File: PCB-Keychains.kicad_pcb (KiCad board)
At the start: 2 copper layers, 79.1 x 91.4 mm, 245 parts

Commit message: Add a bunch of layouts
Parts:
- added REF**: Pad-1U, locallib:Pad-1U, F.Cu at (115.3, 79.1)
- added REF**: Pad-1U, locallib:Pad-1U, F.Cu at (145.7, 79.1)
- added REF**: Pad-1U, locallib:Pad-1U, F.Cu at (174.3, 100.0)
- added REF**: Pad-1U, locallib:Pad-1U, F.Cu at (123.8, 100.0)
- added REF**: Pad-1U, locallib:Pad-1U, F.Cu at (135.3, 100.0)
- added REF**: Pad-2.75U, locallib:Pad-2.75U, F.Cu at (161.4, 100.0)
- added REF**: Pad-1U, locallib:Pad-1U, F.Cu at (146.7, 100.0)
- added REF**: Pad-1U, locallib:Pad-1U, F.Cu at (127.6, 100.0)
- added REF**: Pad-1U, locallib:Pad-1U, F.Cu at (150.5, 100.0)
- added REF**: Pad-1U, locallib:Pad-1U, F.Cu at (178.1, 100.0)
- added REF**: Pad-1U, locallib:Pad-1U, F.Cu at (120.0, 100.0)
- added REF**: Pad-1U, locallib:Pad-1U, F.Cu at (170.5, 88.6)
- added REF**: Pad-1U, locallib:Pad-1U, F.Cu at (119.1, 79.1)
- added REF**: Pad-1.5U, locallib:Pad-1.5U, F.Cu at (121.9, 103.8)
- added REF**: Pad-1U, locallib:Pad-1U, F.Cu at (178.1, 88.6)
- added REF**: Pad-1U, locallib:Pad-1U, F.Cu at (174.3, 88.6)
- added REF**: Pad-1U, locallib:Pad-1U, F.Cu at (131.4, 100.0)
- added REF**: Pad-1U, locallib:Pad-1U, F.Cu at (174.3, 96.2)
- added REF**: Pad-2.25U, locallib:Pad-2.25U, F.Cu at (113.8, 100.0)
- added REF**: Pad-1U, locallib:Pad-1U, F.Cu at (133.3, 96.2)
- added REF**: Pad-1.5U, locallib:Pad-1.5U, F.Cu at (163.8, 103.8)
- added REF**: Pad-1U, locallib:Pad-1U, F.Cu at (170.5, 92.4)
- added REF**: Pad-1U, locallib:Pad-1U, F.Cu at (115.3, 88.6)
- added REF**: Pad-1U, locallib:Pad-1U, F.Cu at (134.3, 79.1)
- added REF**: Pad-1U, locallib:Pad-1U, F.Cu at (226.7, 26.7)
- added REF**: Pad-1U, locallib:Pad-1U, F.Cu at (226.7, 30.5)
- added REF**: Pad-1U, locallib:Pad-1U, F.Cu at (226.7, 19.1)
- added REF**: Pad-1U, locallib:Pad-1U, F.Cu at (230.5, 26.7)
- added REF**: Pad-1U, locallib:Pad-1U, F.Cu at (230.5, 34.3)
- added REF**: Pad-1U, locallib:Pad-1U, F.Cu at (226.7, 22.9)
- added REF**: Pad-1U, locallib:Pad-1U, F.Cu at (230.5, 19.1)
- added REF**: Pad-1U, locallib:Pad-1U, F.Cu at (230.5, 30.5)
- added REF**: Pad-1U, locallib:Pad-1U, F.Cu at (226.7, 34.3)
- added REF**: Pad-1U, locallib:Pad-1U, F.Cu at (230.5, 22.9)
- added REF**: Pad-1U, locallib:Pad-1U, F.Cu at (115.3, 82.9)
- added REF**: Pad-1U, locallib:Pad-1U, F.Cu at (266.7, 30.5)
- added REF**: Pad-1U, locallib:Pad-1U, F.Cu at (255.3, 30.5)
- added REF**: Pad-1U, locallib:Pad-1U, F.Cu at (262.9, 30.5)
- added REF**: Pad-1.5U, locallib:Pad-1.5U, F.Cu at (287.7, 34.3)
- added REF**: Pad-1U, locallib:Pad-1U, F.Cu at (270.5, 30.5)
- added REF**: Pad-1.5U, locallib:Pad-1.5U, F.Cu at (278.1, 34.3)
- added REF**: Pad-1U, locallib:Pad-1U, F.Cu at (259.1, 30.5)
- added REF**: Pad-1.5U, locallib:Pad-1.5U, F.Cu at (236.2, 22.9)
- added REF**: Pad-2.75U, locallib:Pad-2.75U, F.Cu at (285.3, 30.5)
- added REF**: Pad-7U, locallib:Pad-7U, F.Cu at (261.9, 34.3)
- added REF**: Pad-1U, locallib:Pad-1U, F.Cu at (149.5, 82.9)
- added REF**: Pad-1.75U, locallib:Pad-1.75U, F.Cu at (236.7, 26.7)
- added REF**: Pad-1.5U, locallib:Pad-1.5U, F.Cu at (287.7, 22.9)
- added REF**: Pad-2U, locallib:Pad-2U, F.Cu at (286.7, 19.1)
- added REF**: Pad-2.25U, locallib:Pad-2.25U, F.Cu at (286.2, 26.7)
- added REF**: Pad-1.5U, locallib:Pad-1.5U, F.Cu at (236.2, 34.3)
- added REF**: Pad-2.25U, locallib:Pad-2.25U, F.Cu at (237.6, 30.5)
- added REF**: Pad-1.5U, locallib:Pad-1.5U, F.Cu at (245.7, 34.3)
- added REF**: Pad-1U, locallib:Pad-1U, F.Cu at (235.3, 19.1)
- added REF**: Pad-1U, locallib:Pad-1U, F.Cu at (246.7, 19.1)
- added REF**: Pad-1U, locallib:Pad-1U, F.Cu at (242.9, 19.1)
- added REF**: Pad-1U, locallib:Pad-1U, F.Cu at (130.5, 82.9)
- added REF**: Pad-1U, locallib:Pad-1U, F.Cu at (250.5, 19.1)
- added REF**: Pad-1U, locallib:Pad-1U, F.Cu at (277.2, 19.1)
- added REF**: Pad-1U, locallib:Pad-1U, F.Cu at (278.1, 30.5)
- added REF**: Pad-1U, locallib:Pad-1U, F.Cu at (271.5, 22.9)
- added REF**: Pad-1U, locallib:Pad-1U, F.Cu at (263.8, 22.9)
- added REF**: Pad-1U, locallib:Pad-1U, F.Cu at (253.4, 26.7)
- added REF**: Pad-1U, locallib:Pad-1U, F.Cu at (264.8, 26.7)
- added REF**: Pad-1U, locallib:Pad-1U, F.Cu at (261.0, 26.7)
- added REF**: Pad-1U, locallib:Pad-1U, F.Cu at (241.9, 26.7)
- added REF**: Pad-1U, locallib:Pad-1U, F.Cu at (280.0, 26.7)
- added REF**: Pad-1U, locallib:Pad-1U, F.Cu at (122.9, 82.9)
- added REF**: Pad-1U, locallib:Pad-1U, F.Cu at (249.6, 26.7)
- added REF**: Pad-1U, locallib:Pad-1U, F.Cu at (247.7, 30.5)
- added REF**: Pad-1U, locallib:Pad-1U, F.Cu at (274.3, 30.5)
- added REF**: Pad-1U, locallib:Pad-1U, F.Cu at (248.6, 22.9)
- added REF**: Pad-1U, locallib:Pad-1U, F.Cu at (275.3, 22.9)
- added REF**: Pad-1U, locallib:Pad-1U, F.Cu at (256.2, 22.9)
- added REF**: Pad-1U, locallib:Pad-1U, F.Cu at (272.4, 26.7)
- added REF**: Pad-1U, locallib:Pad-1U, F.Cu at (258.1, 19.1)
- added REF**: Pad-1U, locallib:Pad-1U, F.Cu at (261.9, 19.1)
- added REF**: Pad-1U, locallib:Pad-1U, F.Cu at (282.9, 22.9)
- added REF**: Pad-1U, locallib:Pad-1U, F.Cu at (126.7, 82.9)
- added REF**: Pad-1U, locallib:Pad-1U, F.Cu at (257.2, 26.7)
- added REF**: Pad-1U, locallib:Pad-1U, F.Cu at (267.7, 22.9)
- added REF**: Pad-1U, locallib:Pad-1U, F.Cu at (269.6, 19.1)
- added REF**: Pad-1U, locallib:Pad-1U, F.Cu at (243.8, 30.5)
- added REF**: Pad-1U, locallib:Pad-1U, F.Cu at (244.8, 22.9)
- added REF**: Pad-1U, locallib:Pad-1U, F.Cu at (260.0, 22.9)
- added REF**: Pad-1U, locallib:Pad-1U, F.Cu at (252.4, 22.9)
- added REF**: Pad-1U, locallib:Pad-1U, F.Cu at (245.7, 26.7)
- added REF**: Pad-1U, locallib:Pad-1U, F.Cu at (265.7, 19.1)
- added REF**: Pad-1U, locallib:Pad-1U, F.Cu at (268.6, 26.7)
- added REF**: Pad-1U, locallib:Pad-1U, F.Cu at (138.1, 82.9)
- added REF**: Pad-1U, locallib:Pad-1U, F.Cu at (279.1, 22.9)
- added REF**: Pad-1U, locallib:Pad-1U, F.Cu at (251.5, 30.5)
- added REF**: Pad-1U, locallib:Pad-1U, F.Cu at (239.1, 19.1)
- added REF**: Pad-1U, locallib:Pad-1U, F.Cu at (276.2, 26.7)
- added REF**: Pad-1U, locallib:Pad-1U, F.Cu at (254.3, 19.1)
- added REF**: Pad-1U, locallib:Pad-1U, F.Cu at (273.4, 19.1)
- added REF**: Pad-1U, locallib:Pad-1U, F.Cu at (281.0, 19.1)
- added REF**: Pad-1U, locallib:Pad-1U, F.Cu at (241.0, 22.9)
- added REF**: Pad-1.25U, locallib:Pad-1.25U, F.Cu at (97.6, 66.7)
- added REF**: Pad-1.25U, locallib:Pad-1.25U, F.Cu at (135.7, 66.7)
- added REF**: Pad-1U, locallib:Pad-1U, F.Cu at (141.9, 82.9)
- added REF**: Pad-1.25U, locallib:Pad-1.25U, F.Cu at (140.5, 66.7)
- added REF**: Pad-6.25U, locallib:Pad-6.25U, F.Cu at (121.4, 66.7)
- added REF**: Pad-1.25U, locallib:Pad-1.25U, F.Cu at (102.4, 66.7)
- added REF**: Pad-1.25U, locallib:Pad-1.25U, F.Cu at (107.2, 66.7)
- added REF**: Pad-1U, locallib:Pad-1U, F.Cu at (174.3, 58.1)
- added REF**: Pad-1U, locallib:Pad-1U, F.Cu at (204.8, 58.1)
- added REF**: Pad-1U, locallib:Pad-1U, F.Cu at (193.4, 58.1)
- added REF**: Pad-1U, locallib:Pad-1U, F.Cu at (208.6, 58.1)
- added REF**: Pad-1U, locallib:Pad-1U, F.Cu at (197.2, 58.1)
- added REF**: Pad-1U, locallib:Pad-1U, F.Cu at (178.1, 58.1)
- added REF**: Pad-1U, locallib:Pad-1U, F.Cu at (149.5, 79.1)
- added REF**: Pad-1U, locallib:Pad-1U, F.Cu at (157.2, 82.9)
- added REF**: Pad-1U, locallib:Pad-1U, F.Cu at (170.5, 58.1)
- added REF**: Pad-1U, locallib:Pad-1U, F.Cu at (201.0, 58.1)
- added REF**: Pad-1U, locallib:Pad-1U, F.Cu at (181.9, 58.1)
- added REF**: Pad-1U, locallib:Pad-1U, F.Cu at (166.7, 58.1)
- added REF**: Pad-1U, locallib:Pad-1U, F.Cu at (174.3, 54.3)
- added REF**: Pad-1U, locallib:Pad-1U, F.Cu at (204.8, 54.3)
- added REF**: Pad-1U, locallib:Pad-1U, F.Cu at (189.5, 54.3)
- added REF**: Pad-1U, locallib:Pad-1U, F.Cu at (193.4, 54.3)
- added REF**: Pad-1U, locallib:Pad-1U, F.Cu at (208.6, 54.3)
- added REF**: Pad-1U, locallib:Pad-1U, F.Cu at (197.2, 54.3)
- added REF**: Pad-1U, locallib:Pad-1U, F.Cu at (153.4, 82.9)
- added REF**: Pad-1U, locallib:Pad-1U, F.Cu at (178.1, 54.3)
- added REF**: Pad-1U, locallib:Pad-1U, F.Cu at (170.5, 54.3)
- added REF**: Pad-1U, locallib:Pad-1U, F.Cu at (201.0, 54.3)
- added REF**: Pad-1U, locallib:Pad-1U, F.Cu at (181.9, 54.3)
- added REF**: Pad-1U, locallib:Pad-1U, F.Cu at (185.7, 54.3)
- added REF**: Pad-1U, locallib:Pad-1U, F.Cu at (166.7, 54.3)
- added REF**: Pad-1U, locallib:Pad-1U, F.Cu at (174.3, 50.5)
- added REF**: Pad-1U, locallib:Pad-1U, F.Cu at (204.8, 50.5)
- added REF**: Pad-1U, locallib:Pad-1U, F.Cu at (189.5, 50.5)
- added REF**: Pad-1U, locallib:Pad-1U, F.Cu at (193.4, 50.5)
- added REF**: Pad-1U, locallib:Pad-1U, F.Cu at (145.7, 82.9)
- added REF**: Pad-1U, locallib:Pad-1U, F.Cu at (208.6, 50.5)
- added REF**: Pad-1U, locallib:Pad-1U, F.Cu at (197.2, 50.5)
- added REF**: Pad-1U, locallib:Pad-1U, F.Cu at (178.1, 50.5)
- added REF**: Pad-1U, locallib:Pad-1U, F.Cu at (170.5, 50.5)
- added REF**: Pad-1U, locallib:Pad-1U, F.Cu at (201.0, 50.5)
- added REF**: Pad-1U, locallib:Pad-1U, F.Cu at (181.9, 50.5)
- added REF**: Pad-1U, locallib:Pad-1U, F.Cu at (185.7, 50.5)
- added REF**: Pad-1U, locallib:Pad-1U, F.Cu at (166.7, 50.5)
- added REF**: Pad-1U, locallib:Pad-1U, F.Cu at (174.3, 46.7)
- added REF**: Pad-1U, locallib:Pad-1U, F.Cu at (204.8, 46.7)
- added REF**: Pad-1U, locallib:Pad-1U, F.Cu at (119.1, 82.9)
- added REF**: Pad-1U, locallib:Pad-1U, F.Cu at (189.5, 46.7)
- added REF**: Pad-1U, locallib:Pad-1U, F.Cu at (193.4, 46.7)
- added REF**: Pad-1U, locallib:Pad-1U, F.Cu at (208.6, 46.7)
- added REF**: Pad-1U, locallib:Pad-1U, F.Cu at (197.2, 46.7)
- added REF**: Pad-1U, locallib:Pad-1U, F.Cu at (178.1, 46.7)
- added REF**: Pad-1U, locallib:Pad-1U, F.Cu at (170.5, 46.7)
- added REF**: Pad-1U, locallib:Pad-1U, F.Cu at (201.0, 46.7)
- added REF**: Pad-1U, locallib:Pad-1U, F.Cu at (181.9, 46.7)
- added REF**: Pad-1U, locallib:Pad-1U, F.Cu at (185.7, 46.7)
- added REF**: Pad-1U, locallib:Pad-1U, F.Cu at (166.7, 46.7)
- added REF**: Pad-1U, locallib:Pad-1U, F.Cu at (134.3, 82.9)
- added REF**: Pad-1U, locallib:Pad-1U, F.Cu at (106.7, 46.7)
- added REF**: Pad-1U, locallib:Pad-1U, F.Cu at (122.9, 46.7)
- added REF**: Pad-1U, locallib:Pad-1U, F.Cu at (130.5, 46.7)
- added REF**: Pad-1U, locallib:Pad-1U, F.Cu at (142.9, 46.7)
- added REF**: Pad-1U, locallib:Pad-1U, F.Cu at (135.3, 46.7)
- added REF**: Pad-1U, locallib:Pad-1U, F.Cu at (119.1, 46.7)
- added REF**: Pad-1U, locallib:Pad-1U, F.Cu at (146.7, 46.7)
- added REF**: Pad-1U, locallib:Pad-1U, F.Cu at (114.3, 46.7)
- added REF**: Pad-1U, locallib:Pad-1U, F.Cu at (126.7, 46.7)
- added REF**: Pad-1U, locallib:Pad-1U, F.Cu at (139.1, 46.7)
- added REF**: Pad-1U, locallib:Pad-1U, F.Cu at (191.5, 103.8)
- added REF**: Pad-1U, locallib:Pad-1U, F.Cu at (110.5, 46.7)
- added REF**: Pad-1U, locallib:Pad-1U, F.Cu at (102.9, 46.7)
- added REF**: Pad-1U, locallib:Pad-1U, F.Cu at (97.2, 46.7)
- added REF**: Pad-1U, locallib:Pad-1U, F.Cu at (154.3, 59.1)
- added REF**: Pad-1U, locallib:Pad-1U, F.Cu at (154.3, 62.9)
- added REF**: Pad-1.75U, locallib:Pad-1.75U, F.Cu at (145.3, 62.9)
- added REF**: Pad-1U, locallib:Pad-1U, F.Cu at (104.8, 51.4)
- added REF**: Pad-1U, locallib:Pad-1U, F.Cu at (135.3, 51.4)
- added REF**: Pad-1U, locallib:Pad-1U, F.Cu at (114.3, 55.2)
- added REF**: Pad-1U, locallib:Pad-1U, F.Cu at (120.0, 51.4)
- added REF**: Pad-1U, locallib:Pad-1U, F.Cu at (191.5, 96.2)
- added REF**: Pad-1U, locallib:Pad-1U, F.Cu at (154.3, 51.4)
- added REF**: Pad-1U, locallib:Pad-1U, F.Cu at (154.3, 55.2)
- added REF**: Pad-1U, locallib:Pad-1U, F.Cu at (102.9, 55.2)
- added REF**: Pad-2.25U, locallib:Pad-2.25U, F.Cu at (148.1, 59.1)
- added REF**: Pad-1U, locallib:Pad-1U, F.Cu at (125.7, 55.2)
- added REF**: Pad-1U, locallib:Pad-1U, F.Cu at (122.9, 59.1)
- added REF**: Pad-1U, locallib:Pad-1U, F.Cu at (150.5, 62.9)
- added REF**: Pad-1U, locallib:Pad-1U, F.Cu at (150.5, 66.7)
- added REF**: Pad-1U, locallib:Pad-1U, F.Cu at (117.2, 62.9)
- added REF**: Pad-1.5U, locallib:Pad-1.5U, F.Cu at (98.1, 55.2)
- added REF**: Pad-1U, locallib:Pad-1U, F.Cu at (191.5, 88.6)
- added REF**: Pad-1U, locallib:Pad-1U, F.Cu at (123.8, 51.4)
- added REF**: Pad-1U, locallib:Pad-1U, F.Cu at (154.3, 66.7)
- added REF**: Pad-1U, locallib:Pad-1U, F.Cu at (139.1, 51.4)
- added REF**: Pad-1U, locallib:Pad-1U, F.Cu at (127.6, 51.4)
- added REF**: Pad-1U, locallib:Pad-1U, F.Cu at (108.6, 51.4)
- added REF**: Pad-1U, locallib:Pad-1U, F.Cu at (121.9, 55.2)
- added REF**: Pad-1U, locallib:Pad-1U, F.Cu at (144.8, 55.2)
- added REF**: Pad-1U, locallib:Pad-1U, F.Cu at (106.7, 55.2)
- added REF**: Pad-1U, locallib:Pad-1U, F.Cu at (133.3, 55.2)
- added REF**: Pad-2U, locallib:Pad-2U, F.Cu at (148.6, 51.4)
- added REF**: Pad-1U, locallib:Pad-1U, F.Cu at (191.5, 92.4)
- added REF**: Pad-1U, locallib:Pad-1U, F.Cu at (115.3, 59.1)
- added REF**: Pad-1U, locallib:Pad-1U, F.Cu at (101.0, 51.4)
- added REF**: Pad-1U, locallib:Pad-1U, F.Cu at (121.0, 62.9)
- added REF**: Pad-1U, locallib:Pad-1U, F.Cu at (137.2, 55.2)
- added REF**: Pad-1U, locallib:Pad-1U, F.Cu at (107.6, 59.1)
- added REF**: Pad-1U, locallib:Pad-1U, F.Cu at (131.4, 51.4)
- added REF**: Pad-1U, locallib:Pad-1U, F.Cu at (112.4, 51.4)
- added REF**: Pad-1U, locallib:Pad-1U, F.Cu at (132.4, 62.9)
- added REF**: Pad-1U, locallib:Pad-1U, F.Cu at (116.2, 51.4)
- added REF**: Pad-1U, locallib:Pad-1U, F.Cu at (126.7, 59.1)
- added REF**: Pad-1U, locallib:Pad-1U, F.Cu at (191.5, 100.0)
- added REF**: Pad-1U, locallib:Pad-1U, F.Cu at (146.7, 66.7)
- added REF**: Pad-2.25U, locallib:Pad-2.25U, F.Cu at (99.5, 62.9)
- added REF**: Pad-1U, locallib:Pad-1U, F.Cu at (124.8, 62.9)
- added REF**: Pad-1.5U, locallib:Pad-1.5U, F.Cu at (149.5, 55.2)
- added REF**: Pad-1U, locallib:Pad-1U, F.Cu at (109.5, 62.9)
- added REF**: Pad-1U, locallib:Pad-1U, F.Cu at (134.3, 59.1)
- added REF**: Pad-1U, locallib:Pad-1U, F.Cu at (118.1, 55.2)
- added REF**: Pad-1U, locallib:Pad-1U, F.Cu at (97.2, 51.4)
- added REF**: Pad-1U, locallib:Pad-1U, F.Cu at (141.9, 59.1)
- added REF**: Pad-1U, locallib:Pad-1U, F.Cu at (105.7, 62.9)
- added REF**: Pad-1U, locallib:Pad-1U, F.Cu at (130.5, 79.1)
- added REF**: Pad-1U, locallib:Pad-1U, F.Cu at (195.3, 88.6)
- added REF**: Pad-1U, locallib:Pad-1U, F.Cu at (119.1, 59.1)
- added REF**: Pad-1U, locallib:Pad-1U, F.Cu at (111.4, 59.1)
- added REF**: Pad-1U, locallib:Pad-1U, F.Cu at (140.0, 62.9)
- added REF**: Pad-1U, locallib:Pad-1U, F.Cu at (136.2, 62.9)
- added REF**: Pad-1U, locallib:Pad-1U, F.Cu at (113.3, 62.9)
- added REF**: Pad-1U, locallib:Pad-1U, F.Cu at (128.6, 62.9)
- added REF**: Pad-1U, locallib:Pad-1U, F.Cu at (138.1, 59.1)
- added REF**: Pad-1.75U, locallib:Pad-1.75U, F.Cu at (98.6, 59.1)
- added REF**: Pad-1U, locallib:Pad-1U, F.Cu at (130.5, 59.1)
- added REF**: Pad-1U, locallib:Pad-1U, F.Cu at (129.5, 55.2)
- added REF**: Pad-1U, locallib:Pad-1U, F.Cu at (187.6, 103.8)
- added REF**: Pad-1U, locallib:Pad-1U, F.Cu at (141.0, 55.2)
- added REF**: Pad-1U, locallib:Pad-1U, F.Cu at (110.5, 55.2)
- added REF**: Pad-1U, locallib:Pad-1U, F.Cu at (103.8, 59.1)
- added REF**: Pad-1U, locallib:Pad-1U, F.Cu at (142.9, 51.4)
- added REF**: Pad-1U, locallib:Pad-1U, F.Cu at (214.3, 26.7)
- added REF**: Pad-1U, locallib:Pad-1U, F.Cu at (214.3, 30.5)
- added REF**: Pad-1U, locallib:Pad-1U, F.Cu at (168.6, 19.1)
- added REF**: Pad-1U, locallib:Pad-1U, F.Cu at (181.9, 22.9)
- added REF**: Pad-1U, locallib:Pad-1U, F.Cu at (204.8, 22.9)
- added REF**: Pad-1U, locallib:Pad-1U, F.Cu at (191.5, 19.1)
- added REF**: Pad-1U, locallib:Pad-1U, F.Cu at (183.8, 103.8)
- added REF**: Pad-1.5U, locallib:Pad-1.5U, F.Cu at (158.1, 22.9)
- added REF**: Pad-1U, locallib:Pad-1U, F.Cu at (164.8, 19.1)
- added REF**: Pad-1U, locallib:Pad-1U, F.Cu at (195.3, 19.1)
- added REF**: Pad-1U, locallib:Pad-1U, F.Cu at (174.3, 22.9)
- added REF**: Pad-1U, locallib:Pad-1U, F.Cu at (180.0, 19.1)
- added REF**: Pad-1U, locallib:Pad-1U, F.Cu at (172.4, 19.1)
- added REF**: Pad-1U, locallib:Pad-1U, F.Cu at (161.0, 19.1)
- added REF**: Pad-1U, locallib:Pad-1U, F.Cu at (183.8, 19.1)
- added REF**: Pad-1U, locallib:Pad-1U, F.Cu at (176.2, 19.1)
- added REF**: Pad-1U, locallib:Pad-1U, F.Cu at (166.7, 22.9)
- added REF**: Pad-1U, locallib:Pad-1U, F.Cu at (183.8, 96.2)
- added REF**: Pad-1U, locallib:Pad-1U, F.Cu at (199.1, 19.1)
- added REF**: Pad-1U, locallib:Pad-1U, F.Cu at (210.5, 30.5)
- added REF**: Pad-1U, locallib:Pad-1U, F.Cu at (214.3, 19.1)
- added REF**: Pad-1U, locallib:Pad-1U, F.Cu at (193.4, 22.9)
- added REF**: Pad-1U, locallib:Pad-1U, F.Cu at (210.5, 34.3)
- added REF**: Pad-1U, locallib:Pad-1U, F.Cu at (214.3, 34.3)
- added REF**: Pad-1U, locallib:Pad-1U, F.Cu at (206.7, 34.3)
- added REF**: Pad-1U, locallib:Pad-1U, F.Cu at (214.3, 22.9)
- added REF**: Pad-1U, locallib:Pad-1U, F.Cu at (162.9, 22.9)
- added REF**: Pad-1U, locallib:Pad-1U, F.Cu at (187.6, 19.1)
- added REF**: Pad-1U, locallib:Pad-1U, F.Cu at (187.6, 100.0)
- added REF**: Pad-2.25U, locallib:Pad-2.25U, F.Cu at (159.5, 30.5)
- added REF**: Pad-1U, locallib:Pad-1U, F.Cu at (177.2, 30.5)
- added REF**: Pad-1U, locallib:Pad-1U, F.Cu at (181.0, 30.5)
- added REF**: Pad-1U, locallib:Pad-1U, F.Cu at (192.4, 30.5)
- added REF**: Pad-2.25U, locallib:Pad-2.25U, F.Cu at (208.1, 26.7)
- added REF**: Pad-2U, locallib:Pad-2U, F.Cu at (208.6, 19.1)
- added REF**: Pad-1U, locallib:Pad-1U, F.Cu at (186.7, 26.7)
- added REF**: Pad-1U, locallib:Pad-1U, F.Cu at (185.7, 22.9)
- added REF**: Pad-1U, locallib:Pad-1U, F.Cu at (197.2, 22.9)
- added REF**: Pad-1U, locallib:Pad-1U, F.Cu at (182.9, 26.7)
- added REF**: Pad-1U, locallib:Pad-1U, F.Cu at (183.8, 88.6)
- added REF**: Pad-1U, locallib:Pad-1U, F.Cu at (167.6, 26.7)
- added REF**: Pad-1U, locallib:Pad-1U, F.Cu at (175.3, 26.7)
- added REF**: Pad-1U, locallib:Pad-1U, F.Cu at (184.8, 30.5)
- added REF**: Pad-1U, locallib:Pad-1U, F.Cu at (194.3, 26.7)
- added REF**: Pad-1U, locallib:Pad-1U, F.Cu at (178.1, 22.9)
- added REF**: Pad-1U, locallib:Pad-1U, F.Cu at (157.2, 19.1)
- added REF**: Pad-1U, locallib:Pad-1U, F.Cu at (201.9, 26.7)
- added REF**: Pad-1U, locallib:Pad-1U, F.Cu at (165.7, 30.5)
- added REF**: Pad-1U, locallib:Pad-1U, F.Cu at (169.5, 30.5)
- added REF**: Pad-1U, locallib:Pad-1U, F.Cu at (179.1, 26.7)
- added REF**: Pad-1U, locallib:Pad-1U, F.Cu at (183.8, 92.4)
- added REF**: Pad-1.5U, locallib:Pad-1.5U, F.Cu at (209.6, 22.9)
- added REF**: Pad-1U, locallib:Pad-1U, F.Cu at (201.0, 22.9)
- added REF**: Pad-1U, locallib:Pad-1U, F.Cu at (171.4, 26.7)
- added REF**: Pad-1U, locallib:Pad-1U, F.Cu at (200.0, 30.5)
- added REF**: Pad-1U, locallib:Pad-1U, F.Cu at (196.2, 30.5)
- added REF**: Pad-1U, locallib:Pad-1U, F.Cu at (173.4, 30.5)
- added REF**: Pad-1U, locallib:Pad-1U, F.Cu at (188.6, 30.5)
- added REF**: Pad-1U, locallib:Pad-1U, F.Cu at (198.1, 26.7)
- added REF**: Pad-1U, locallib:Pad-1U, F.Cu at (170.5, 22.9)
- added REF**: Pad-1.75U, locallib:Pad-1.75U, F.Cu at (158.6, 26.7)
- added REF**: Pad-1U, locallib:Pad-1U, F.Cu at (187.6, 96.2)
- added REF**: Pad-1U, locallib:Pad-1U, F.Cu at (190.5, 26.7)
- added REF**: Pad-1U, locallib:Pad-1U, F.Cu at (163.8, 26.7)
- added REF**: Pad-1U, locallib:Pad-1U, F.Cu at (189.5, 22.9)
- added REF**: Pad-1U, locallib:Pad-1U, F.Cu at (202.9, 19.1)
- added REF**: Pad-1.25U, locallib:Pad-1.25U, F.Cu at (132.9, 34.3)
- added REF**: Pad-1.25U, locallib:Pad-1.25U, F.Cu at (128.1, 34.3)
- added REF**: Pad-1.25U, locallib:Pad-1.25U, F.Cu at (123.3, 34.3)
- added REF**: Pad-1U, locallib:Pad-1U, F.Cu at (131.4, 19.1)
- added REF**: Pad-1U, locallib:Pad-1U, F.Cu at (118.1, 22.9)
- added REF**: Pad-1U, locallib:Pad-1U, F.Cu at (95.2, 22.9)
- added REF**: Pad-1U, locallib:Pad-1U, F.Cu at (183.8, 100.0)
- added REF**: Pad-1U, locallib:Pad-1U, F.Cu at (110.5, 22.9)
- added REF**: Pad-1U, locallib:Pad-1U, F.Cu at (102.9, 22.9)
- added REF**: Pad-1.5U, locallib:Pad-1.5U, F.Cu at (86.7, 22.9)
- added REF**: Pad-1U, locallib:Pad-1U, F.Cu at (133.3, 22.9)
- added REF**: Pad-1U, locallib:Pad-1U, F.Cu at (127.6, 19.1)
- added REF**: Pad-1U, locallib:Pad-1U, F.Cu at (97.2, 19.1)
- added REF**: Pad-1U, locallib:Pad-1U, F.Cu at (108.6, 19.1)
- added REF**: Pad-1U, locallib:Pad-1U, F.Cu at (120.0, 19.1)
- added REF**: Pad-1U, locallib:Pad-1U, F.Cu at (123.8, 19.1)
- added REF**: Pad-1U, locallib:Pad-1U, F.Cu at (101.0, 19.1)
- added REF**: Pad-1U, locallib:Pad-1U, F.Cu at (187.6, 88.6)
- added REF**: Pad-1U, locallib:Pad-1U, F.Cu at (112.4, 19.1)
- added REF**: Pad-1U, locallib:Pad-1U, F.Cu at (104.8, 19.1)
- added REF**: Pad-1U, locallib:Pad-1U, F.Cu at (93.3, 19.1)
- added REF**: Pad-1U, locallib:Pad-1U, F.Cu at (89.5, 19.1)
- added REF**: Pad-1U, locallib:Pad-1U, F.Cu at (144.8, 19.1)
- added REF**: Pad-1U, locallib:Pad-1U, F.Cu at (141.0, 30.5)
- added REF**: Pad-1U, locallib:Pad-1U, F.Cu at (144.8, 34.3)
- added REF**: Pad-1U, locallib:Pad-1U, F.Cu at (141.0, 34.3)
- added REF**: Pad-1U, locallib:Pad-1U, F.Cu at (137.2, 34.3)
- added REF**: Pad-1U, locallib:Pad-1U, F.Cu at (144.8, 22.9)
- added REF**: Pad-1U, locallib:Pad-1U, F.Cu at (122.9, 79.1)
- added REF**: Pad-1U, locallib:Pad-1U, F.Cu at (187.6, 92.4)
- added REF**: Pad-2.25U, locallib:Pad-2.25U, F.Cu at (88.1, 30.5)
- added REF**: Pad-1U, locallib:Pad-1U, F.Cu at (105.7, 30.5)
- added REF**: Pad-1U, locallib:Pad-1U, F.Cu at (109.5, 30.5)
- added REF**: Pad-1U, locallib:Pad-1U, F.Cu at (121.0, 30.5)
- added REF**: Pad-2.25U, locallib:Pad-2.25U, F.Cu at (136.7, 26.7)
- added REF**: Pad-2U, locallib:Pad-2U, F.Cu at (137.2, 19.1)
- added REF**: Pad-1U, locallib:Pad-1U, F.Cu at (91.4, 22.9)
- added REF**: Pad-1U, locallib:Pad-1U, F.Cu at (116.2, 19.1)
- added REF**: Pad-1U, locallib:Pad-1U, F.Cu at (111.4, 26.7)
- added REF**: Pad-1U, locallib:Pad-1U, F.Cu at (121.9, 22.9)
- added REF**: Pad-1U, locallib:Pad-1U, F.Cu at (174.3, 103.8)
- added REF**: Pad-1U, locallib:Pad-1U, F.Cu at (96.2, 26.7)
- added REF**: Pad-1U, locallib:Pad-1U, F.Cu at (103.8, 26.7)
- added REF**: Pad-1U, locallib:Pad-1U, F.Cu at (92.4, 26.7)
- added REF**: Pad-1U, locallib:Pad-1U, F.Cu at (106.7, 22.9)
- added REF**: Pad-1U, locallib:Pad-1U, F.Cu at (107.6, 26.7)
- added REF**: Pad-1.5U, locallib:Pad-1.5U, F.Cu at (138.1, 22.9)
- added REF**: Pad-1U, locallib:Pad-1U, F.Cu at (113.3, 30.5)
- added REF**: Pad-1.75U, locallib:Pad-1.75U, F.Cu at (87.2, 26.7)
- added REF**: Pad-1U, locallib:Pad-1U, F.Cu at (98.1, 30.5)
- added REF**: Pad-1U, locallib:Pad-1U, F.Cu at (85.7, 19.1)
- added REF**: Pad-1U, locallib:Pad-1U, F.Cu at (101.9, 88.6)
- added REF**: Pad-1U, locallib:Pad-1U, F.Cu at (122.9, 26.7)
- added REF**: Pad-1U, locallib:Pad-1U, F.Cu at (119.1, 26.7)
- added REF**: Pad-1U, locallib:Pad-1U, F.Cu at (114.3, 22.9)
- added REF**: Pad-1U, locallib:Pad-1U, F.Cu at (99.1, 22.9)
- added REF**: Pad-1U, locallib:Pad-1U, F.Cu at (129.5, 22.9)
- added REF**: Pad-1U, locallib:Pad-1U, F.Cu at (126.7, 26.7)
- added REF**: Pad-1U, locallib:Pad-1U, F.Cu at (101.9, 30.5)
- added REF**: Pad-1U, locallib:Pad-1U, F.Cu at (117.2, 30.5)
- added REF**: Pad-1U, locallib:Pad-1U, F.Cu at (115.3, 26.7)
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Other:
- board size 79.1 x 91.4 mm -> 278.1 x 93.3 mm

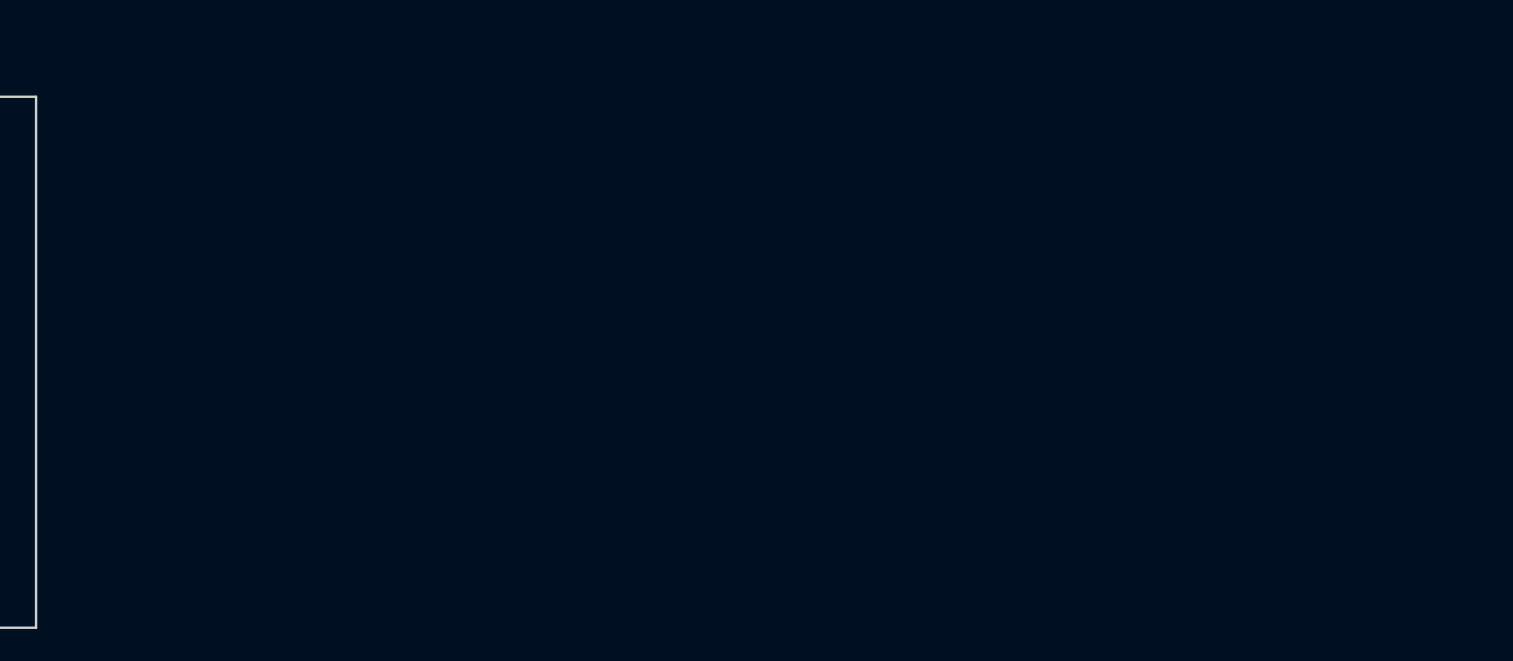
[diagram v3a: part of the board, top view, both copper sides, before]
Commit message: Add Wyse 60
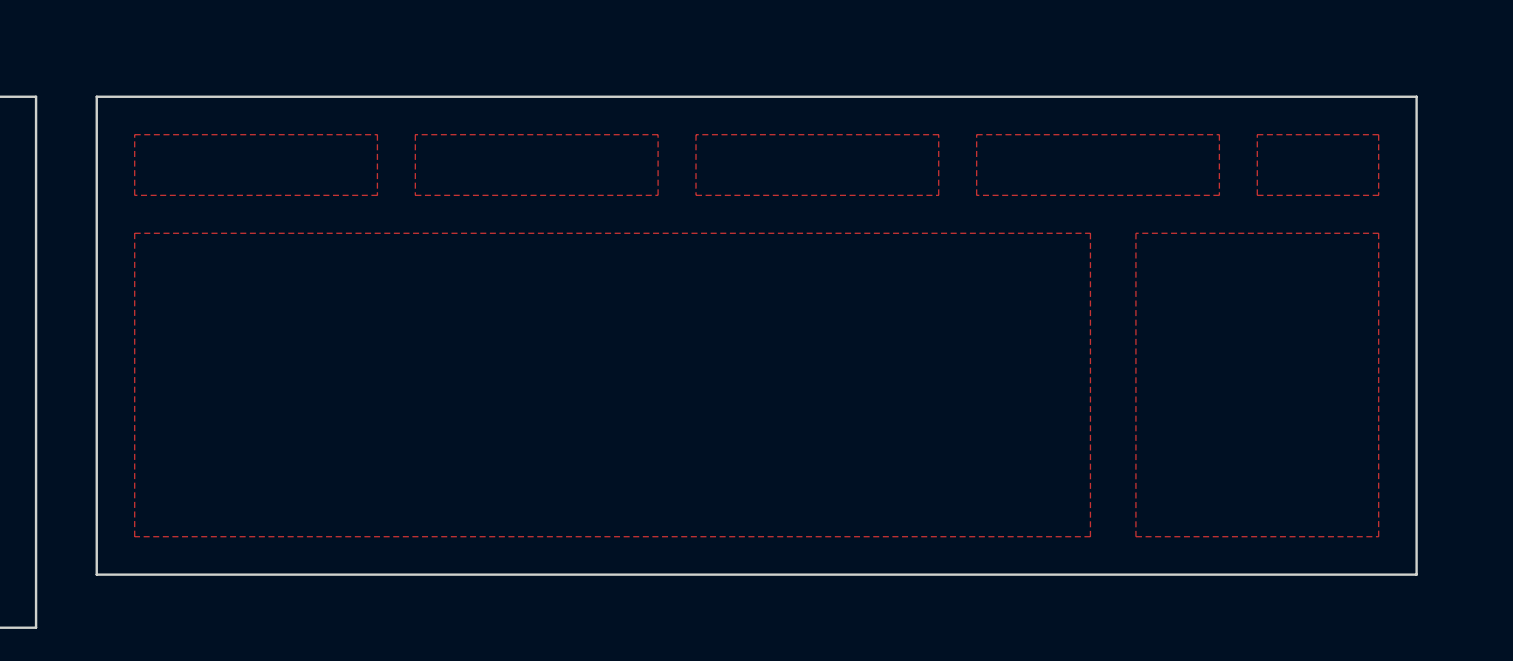
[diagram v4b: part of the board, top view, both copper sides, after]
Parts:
- added REF**: Pad-1.5U, locallib:Pad-1.5U, F.Cu at (208.6, 89.1)
- added REF**: Pad-1U, locallib:Pad-1U, F.Cu at (245.7, 85.2)
- added REF**: Pad-1U, locallib:Pad-1U, F.Cu at (248.6, 92.9)
- added REF**: Pad-1U, locallib:Pad-1U, F.Cu at (214.3, 92.9)
- added REF**: Pad-1U, locallib:Pad-1U, F.Cu at (241.0, 92.9)
- added REF**: Pad-1U, locallib:Pad-1U, F.Cu at (223.8, 96.7)
- added REF**: Pad-1U, locallib:Pad-1U, F.Cu at (240.0, 89.1)
- added REF**: Pad-1U, locallib:Pad-1U, F.Cu at (250.5, 96.7)
- added REF**: Pad-1U, locallib:Pad-1U, F.Cu at (239.1, 96.7)
- added REF**: Pad-1.75U, locallib:Pad-1.75U, F.Cu at (209.1, 92.9)
- added REF**: Pad-1U, locallib:Pad-1U, F.Cu at (253.4, 85.2)
- added REF**: Pad-1U, locallib:Pad-1U, F.Cu at (263.8, 96.7)
- added REF**: Pad-1U, locallib:Pad-1U, F.Cu at (251.5, 89.1)
- added REF**: Pad-1U, locallib:Pad-1U, F.Cu at (221.0, 89.1)
- added REF**: Pad-1U, locallib:Pad-1U, F.Cu at (221.9, 92.9)
- added REF**: Pad-1U, locallib:Pad-1U, F.Cu at (246.7, 96.7)
- added REF**: Pad-1U, locallib:Pad-1U, F.Cu at (218.1, 92.9)
- added REF**: Pad-1U, locallib:Pad-1U, F.Cu at (263.8, 100.5)
- added REF**: Pad-1U, locallib:Pad-1U, F.Cu at (247.7, 89.1)
- added REF**: Pad-1U, locallib:Pad-1U, F.Cu at (259.1, 89.1)
- added REF**: Pad-1U, locallib:Pad-1U, F.Cu at (243.8, 89.1)
- added REF**: Pad-1U, locallib:Pad-1U, F.Cu at (263.8, 85.2)
- added REF**: Pad-1U, locallib:Pad-1U, F.Cu at (232.4, 89.1)
- added REF**: Pad-1U, locallib:Pad-1U, F.Cu at (222.9, 85.2)
- added REF**: Pad-1U, locallib:Pad-1U, F.Cu at (230.5, 85.2)
- added REF**: Pad-1U, locallib:Pad-1U, F.Cu at (229.6, 92.9)
- added REF**: Pad-1U, locallib:Pad-1U, F.Cu at (220.0, 96.7)
- added REF**: Pad-1U, locallib:Pad-1U, F.Cu at (216.2, 96.7)
- added REF**: Pad-1U, locallib:Pad-1U, F.Cu at (237.2, 92.9)
- added REF**: Pad-1U, locallib:Pad-1U, F.Cu at (236.2, 89.1)
- added REF**: Pad-1U, locallib:Pad-1U, F.Cu at (260.0, 96.7)
- added REF**: Pad-1U, locallib:Pad-1U, F.Cu at (252.4, 92.9)
- added REF**: Pad-1U, locallib:Pad-1U, F.Cu at (207.6, 85.2)
- added REF**: Pad-1U, locallib:Pad-1U, F.Cu at (263.8, 92.9)
- added REF**: Pad-1U, locallib:Pad-1U, F.Cu at (217.2, 89.1)
- added REF**: Pad-1U, locallib:Pad-1U, F.Cu at (228.6, 89.1)
- added REF**: Pad-1U, locallib:Pad-1U, F.Cu at (233.4, 92.9)
- added REF**: Pad-1U, locallib:Pad-1U, F.Cu at (244.8, 92.9)
- added REF**: Pad-1U, locallib:Pad-1U, F.Cu at (256.2, 100.5)
- added REF**: Pad-1U, locallib:Pad-1U, F.Cu at (213.4, 89.1)
- added REF**: Pad-1U, locallib:Pad-1U, F.Cu at (227.6, 96.7)
- added REF**: Pad-1U, locallib:Pad-1U, F.Cu at (260.0, 100.5)
- added REF**: Pad-1U, locallib:Pad-1U, F.Cu at (231.5, 96.7)
- added REF**: Pad-1U, locallib:Pad-1U, F.Cu at (238.1, 85.2)
- added REF**: Pad-1U, locallib:Pad-1U, F.Cu at (224.8, 89.1)
- added REF**: Pad-2.25U, locallib:Pad-2.25U, F.Cu at (210.0, 96.7)
- added REF**: Pad-1U, locallib:Pad-1U, F.Cu at (211.5, 85.2)
- added REF**: Pad-1U, locallib:Pad-1U, F.Cu at (249.6, 85.2)
- added REF**: Pad-1U, locallib:Pad-1U, F.Cu at (235.3, 96.7)
- added REF**: Pad-1U, locallib:Pad-1U, F.Cu at (225.7, 92.9)
- added REF**: Pad-1U, locallib:Pad-1U, F.Cu at (242.9, 96.7)
- added REF**: Pad-1U, locallib:Pad-1U, F.Cu at (226.7, 85.2)
- added REF**: Pad-1U, locallib:Pad-1U, F.Cu at (234.3, 85.2)
- added REF**: Pad-1U, locallib:Pad-1U, F.Cu at (281.9, 89.1)
- added REF**: Pad-1U, locallib:Pad-1U, F.Cu at (278.1, 92.9)
- added REF**: Pad-1U, locallib:Pad-1U, F.Cu at (241.9, 85.2)
- added REF**: Pad-1U, locallib:Pad-1U, F.Cu at (278.1, 85.2)
- added REF**: Pad-1U, locallib:Pad-1U, F.Cu at (278.1, 96.7)
- added REF**: Pad-1U, locallib:Pad-1U, F.Cu at (281.9, 85.2)
- added REF**: Pad-1U, locallib:Pad-1U, F.Cu at (281.9, 92.9)
- added REF**: Pad-1U, locallib:Pad-1U, F.Cu at (270.5, 92.9)
- added REF**: Pad-1U, locallib:Pad-1U, F.Cu at (274.3, 96.7)
- added REF**: Pad-1U, locallib:Pad-1U, F.Cu at (270.5, 89.1)
- added REF**: Pad-1U, locallib:Pad-1U, F.Cu at (274.3, 92.9)
- added REF**: Pad-2U, locallib:Pad-2U, F.Cu at (281.9, 98.6)
- added REF**: Pad-1U, locallib:Pad-1U, F.Cu at (270.5, 85.2)
- added REF**: Pad-1U, locallib:Pad-1U, F.Cu at (255.3, 89.1)
- added REF**: Pad-1U, locallib:Pad-1U, F.Cu at (278.1, 89.1)
- added REF**: Pad-1U, locallib:Pad-1U, F.Cu at (270.5, 96.7)
- added REF**: Pad-1U, locallib:Pad-1U, F.Cu at (278.1, 100.5)
- added REF**: Pad-2U, locallib:Pad-2U, F.Cu at (272.4, 100.5)
- added REF**: Pad-1U, locallib:Pad-1U, F.Cu at (274.3, 85.2)
- added REF**: Pad-1U, locallib:Pad-1U, F.Cu at (274.3, 89.1)
- added REF**: Pad-1U, locallib:Pad-1U, F.Cu at (278.1, 79.1)
- added REF**: Pad-1U, locallib:Pad-1U, F.Cu at (281.9, 79.1)
- added REF**: Pad-1U, locallib:Pad-1U, F.Cu at (264.3, 79.1)
- added REF**: Pad-1.75U, locallib:Pad-1.75U, F.Cu at (258.6, 85.2)
- added REF**: Pad-1U, locallib:Pad-1U, F.Cu at (271.9, 79.1)
- added REF**: Pad-1.25U, locallib:Pad-1.25U, F.Cu at (263.4, 89.1)
- added REF**: Pad-2U, locallib:Pad-2U, F.Cu at (258.1, 92.9)
- added REF**: Pad-1.5U, locallib:Pad-1.5U, F.Cu at (255.3, 96.7)
- added REF**: Pad-1U, locallib:Pad-1U, F.Cu at (252.4, 100.5)
- added REF**: Pad-9.75U, locallib:Pad-9.75U, F.Cu at (231.9, 100.5)
- added REF**: Pad-2U, locallib:Pad-2U, F.Cu at (209.6, 100.5)
- added REF**: Pad-1U, locallib:Pad-1U, F.Cu at (219.1, 85.2)
- added REF**: Pad-1U, locallib:Pad-1U, F.Cu at (268.1, 79.1)
- added REF**: Pad-1U, locallib:Pad-1U, F.Cu at (260.5, 79.1)
- added REF**: Pad-1U, locallib:Pad-1U, F.Cu at (242.9, 79.1)
- added REF**: Pad-1U, locallib:Pad-1U, F.Cu at (250.5, 79.1)
- added REF**: Pad-1U, locallib:Pad-1U, F.Cu at (254.3, 79.1)
- added REF**: Pad-1U, locallib:Pad-1U, F.Cu at (246.7, 79.1)
- added REF**: Pad-1U, locallib:Pad-1U, F.Cu at (232.9, 79.1)
- added REF**: Pad-1U, locallib:Pad-1U, F.Cu at (236.7, 79.1)
- added REF**: Pad-1U, locallib:Pad-1U, F.Cu at (225.3, 79.1)
- added REF**: Pad-1U, locallib:Pad-1U, F.Cu at (229.1, 79.1)
- added REF**: Pad-1U, locallib:Pad-1U, F.Cu at (215.3, 85.2)
- added REF**: Pad-1U, locallib:Pad-1U, F.Cu at (215.3, 79.1)
- added REF**: Pad-1U, locallib:Pad-1U, F.Cu at (219.1, 79.1)
- added REF**: Pad-1U, locallib:Pad-1U, F.Cu at (207.6, 79.1)
- added REF**: Pad-1U, locallib:Pad-1U, F.Cu at (211.5, 79.1)
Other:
- outline, holes or cut-outs redrawn
- board text added: "Mechanical Keyboards 122-key ANSI"
- board text added: "Mechanical Keyboards 60% ANSI"
- board text added: "Mechanical Keyboards 60% WKL with vertical function keys"
- board text added: "Mechanical Keyboards 65% with blocker"
- board text added: "Mechanical Keyboards 75% with blocker"
- board text added: "Mechanical Keyboards ANSI WKL TKL"
- board text added: "Mechanical Keyboards FC660"
- board text added: "Mechanical Keyboards G80-1800"
- board text added: "Mechanical Keyboards Planck/40% Ortholinear"
- board text added: "Mechanical Keyboards Wyse 60"

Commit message: Add Ergodox, Let's Split
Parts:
- added REF**: Pad-1U, locallib:Pad-1U, F.Cu at (351.5, 19.1)
- added REF**: Pad-1U, locallib:Pad-1U, F.Cu at (343.9, 19.1)
- added REF**: Pad-1U, locallib:Pad-1U, F.Cu at (291.9, 59.5)
- added REF**: Pad-1U, locallib:Pad-1U, F.Cu at (291.9, 55.7)
- added REF**: Pad-1U, locallib:Pad-1U, F.Cu at (284.3, 59.5)
- added REF**: Pad-1U, locallib:Pad-1U, F.Cu at (284.3, 55.7)
- added REF**: Pad-1U, locallib:Pad-1U, F.Cu at (351.5, 26.7)
- added REF**: Pad-1U, locallib:Pad-1U, F.Cu at (336.2, 26.7)
- added REF**: Pad-1U, locallib:Pad-1U, F.Cu at (347.7, 26.7)
- added REF**: Pad-1U, locallib:Pad-1U, F.Cu at (340.0, 22.9)
- added REF**: Pad-1U, locallib:Pad-1U, F.Cu at (336.2, 30.5)
- added REF**: Pad-1U, locallib:Pad-1U, F.Cu at (347.7, 30.5)
- added REF**: Pad-1U, locallib:Pad-1U, F.Cu at (343.9, 22.9)
- added REF**: Pad-1U, locallib:Pad-1U, F.Cu at (332.4, 30.5)
- added REF**: Pad-1U, locallib:Pad-1U, F.Cu at (347.7, 19.1)
- added REF**: Pad-1U, locallib:Pad-1U, F.Cu at (351.5, 22.9)
- added REF**: Pad-1U, locallib:Pad-1U, F.Cu at (340.0, 26.7)
- added REF**: Pad-1U, locallib:Pad-1U, F.Cu at (347.7, 22.9)
- added REF**: Pad-1U, locallib:Pad-1U, F.Cu at (340.0, 30.5)
- added REF**: Pad-1U, locallib:Pad-1U, F.Cu at (336.2, 22.9)
- added REF**: Pad-1U, locallib:Pad-1U, F.Cu at (343.9, 30.5)
- added REF**: Pad-1U, locallib:Pad-1U, F.Cu at (304.8, 19.1)
- added REF**: Pad-1U, locallib:Pad-1U, F.Cu at (320.0, 19.1)
- added REF**: Pad-1U, locallib:Pad-1U, F.Cu at (320.0, 22.9)
- added REF**: Pad-1U, locallib:Pad-1U, F.Cu at (316.2, 19.1)
- added REF**: Pad-1U, locallib:Pad-1U, F.Cu at (301.0, 22.9)
- added REF**: Pad-1U, locallib:Pad-1U, F.Cu at (351.5, 30.5)
- added REF**: Pad-1U, locallib:Pad-1U, F.Cu at (301.0, 19.1)
- added REF**: Pad-1U, locallib:Pad-1U, F.Cu at (308.6, 19.1)
- added REF**: Pad-1U, locallib:Pad-1U, F.Cu at (312.4, 19.1)
- added REF**: Pad-1U, locallib:Pad-1U, F.Cu at (301.0, 26.7)
- added REF**: Pad-1U, locallib:Pad-1U, F.Cu at (312.4, 22.9)
- added REF**: Pad-1U, locallib:Pad-1U, F.Cu at (320.0, 26.7)
- added REF**: Pad-1U, locallib:Pad-1U, F.Cu at (304.8, 26.7)
- added REF**: Pad-1U, locallib:Pad-1U, F.Cu at (312.4, 26.7)
- added REF**: Pad-1U, locallib:Pad-1U, F.Cu at (316.2, 26.7)
- added REF**: Pad-1U, locallib:Pad-1U, F.Cu at (304.8, 22.9)
- added REF**: Pad-1U, locallib:Pad-1U, F.Cu at (336.2, 19.1)
- added REF**: Pad-1U, locallib:Pad-1U, F.Cu at (316.2, 22.9)
- added REF**: Pad-1U, locallib:Pad-1U, F.Cu at (308.6, 22.9)
- added REF**: Pad-1U, locallib:Pad-1U, F.Cu at (316.2, 30.5)
- added REF**: Pad-1U, locallib:Pad-1U, F.Cu at (304.8, 30.5)
- added REF**: Pad-1U, locallib:Pad-1U, F.Cu at (312.4, 30.5)
- added REF**: Pad-1U, locallib:Pad-1U, F.Cu at (308.6, 30.5)
- added REF**: Pad-1U, locallib:Pad-1U, F.Cu at (308.6, 26.7)
- added REF**: Pad-1U, locallib:Pad-1U, F.Cu at (301.0, 30.5)
- added REF**: Pad-1U, locallib:Pad-1U, F.Cu at (321.9, 71.2)
- added REF**: Pad-1U, locallib:Pad-1U, F.Cu at (318.2, 64.6)
- added REF**: Pad-1U, locallib:Pad-1U, F.Cu at (332.4, 26.7)
- added REF**: Pad-1U, locallib:Pad-1U, F.Cu at (321.5, 62.7)
- added REF**: Pad-1U, locallib:Pad-1U, F.Cu at (320.1, 67.9)
- added REF**: Pad-2U, locallib:Pad-2U, F.Cu at (324.3, 67.6)
- added REF**: Pad-2U, locallib:Pad-2U, F.Cu at (327.7, 65.7)
- added REF**: Pad-1.5U, locallib:Pad-1.5U, F.Cu at (345.3, 49.1)
- added REF**: Pad-1.5U, locallib:Pad-1.5U, F.Cu at (345.3, 56.7)
- added REF**: Pad-1.5U, locallib:Pad-1.5U, F.Cu at (345.3, 60.5)
- added REF**: Pad-1U, locallib:Pad-1U, F.Cu at (344.3, 64.3)
- added REF**: Pad-1U, locallib:Pad-1U, F.Cu at (336.7, 63.3)
- added REF**: Pad-1U, locallib:Pad-1U, F.Cu at (340.5, 64.3)
- added REF**: Pad-1U, locallib:Pad-1U, F.Cu at (343.9, 26.7)
- added REF**: Pad-1U, locallib:Pad-1U, F.Cu at (332.9, 62.9)
- added REF**: Pad-1.5U, locallib:Pad-1.5U, F.Cu at (345.3, 52.9)
- added REF**: Pad-1U, locallib:Pad-1U, F.Cu at (340.5, 60.5)
- added REF**: Pad-1U, locallib:Pad-1U, F.Cu at (340.5, 56.7)
- added REF**: Pad-1U, locallib:Pad-1U, F.Cu at (329.1, 48.1)
- added REF**: Pad-1U, locallib:Pad-1U, F.Cu at (332.9, 55.2)
- added REF**: Pad-1U, locallib:Pad-1U, F.Cu at (340.5, 52.9)
- added REF**: Pad-1U, locallib:Pad-1U, F.Cu at (340.5, 49.1)
- added REF**: Pad-1U, locallib:Pad-1U, F.Cu at (332.9, 51.4)
- added REF**: Pad-1U, locallib:Pad-1U, F.Cu at (325.3, 48.6)
- added REF**: Pad-1U, locallib:Pad-1U, F.Cu at (332.4, 22.9)
- added REF**: Pad-1U, locallib:Pad-1U, F.Cu at (332.9, 47.6)
- added REF**: Pad-1U, locallib:Pad-1U, F.Cu at (336.7, 51.9)
- added REF**: Pad-1U, locallib:Pad-1U, F.Cu at (329.1, 51.9)
- added REF**: Pad-1U, locallib:Pad-1U, F.Cu at (336.7, 48.1)
- added REF**: Pad-1U, locallib:Pad-1U, F.Cu at (325.3, 56.2)
- added REF**: Pad-1U, locallib:Pad-1U, F.Cu at (325.3, 52.4)
- added REF**: Pad-1U, locallib:Pad-1U, F.Cu at (336.7, 55.7)
- added REF**: Pad-1U, locallib:Pad-1U, F.Cu at (332.9, 59.1)
- added REF**: Pad-1U, locallib:Pad-1U, F.Cu at (325.3, 60.0)
- added REF**: Pad-1U, locallib:Pad-1U, F.Cu at (329.1, 59.5)
- added REF**: Pad-1U, locallib:Pad-1U, F.Cu at (332.4, 19.1)
- added REF**: Pad-1U, locallib:Pad-1U, F.Cu at (329.1, 55.7)
- added REF**: Pad-1U, locallib:Pad-1U, F.Cu at (336.7, 59.5)
- added REF**: Pad-1U, locallib:Pad-1U, F.Cu at (280.5, 64.3)
- added REF**: Pad-1U, locallib:Pad-1U, F.Cu at (288.1, 62.9)
- added REF**: Pad-1U, locallib:Pad-1U, F.Cu at (284.3, 63.3)
- added REF**: Pad-1U, locallib:Pad-1U, F.Cu at (284.3, 48.1)
- added REF**: Pad-1U, locallib:Pad-1U, F.Cu at (288.1, 47.6)
- added REF**: Pad-1U, locallib:Pad-1U, F.Cu at (295.8, 48.6)
- added REF**: Pad-1U, locallib:Pad-1U, F.Cu at (280.5, 49.1)
- added REF**: Pad-1U, locallib:Pad-1U, F.Cu at (291.9, 48.1)
- added REF**: Pad-1U, locallib:Pad-1U, F.Cu at (280.5, 60.5)
- added REF**: Pad-1U, locallib:Pad-1U, F.Cu at (340.0, 19.1)
- added REF**: Pad-1U, locallib:Pad-1U, F.Cu at (291.9, 51.9)
- added REF**: Pad-1U, locallib:Pad-1U, F.Cu at (276.7, 64.3)
- added REF**: Pad-1.5U, locallib:Pad-1.5U, F.Cu at (275.7, 60.5)
- added REF**: Pad-1.5U, locallib:Pad-1.5U, F.Cu at (275.7, 56.7)
- added REF**: Pad-1.5U, locallib:Pad-1.5U, F.Cu at (275.7, 52.9)
- added REF**: Pad-1.5U, locallib:Pad-1.5U, F.Cu at (275.7, 49.1)
- added REF**: Pad-2U, locallib:Pad-2U, F.Cu at (293.4, 65.7)
- added REF**: Pad-2U, locallib:Pad-2U, F.Cu at (296.7, 67.6)
- added REF**: Pad-1U, locallib:Pad-1U, F.Cu at (299.6, 62.7)
- added REF**: Pad-1U, locallib:Pad-1U, F.Cu at (302.9, 64.6)
- added REF**: Pad-1U, locallib:Pad-1U, F.Cu at (301.0, 67.9)
- added REF**: Pad-1U, locallib:Pad-1U, F.Cu at (288.1, 51.4)
- added REF**: Pad-1U, locallib:Pad-1U, F.Cu at (299.1, 71.2)
- added REF**: Pad-1U, locallib:Pad-1U, F.Cu at (320.0, 30.5)
- added REF**: Pad-1U, locallib:Pad-1U, F.Cu at (288.1, 55.2)
- added REF**: Pad-1U, locallib:Pad-1U, F.Cu at (284.3, 51.9)
- added REF**: Pad-1U, locallib:Pad-1U, F.Cu at (280.5, 52.9)
- added REF**: Pad-1U, locallib:Pad-1U, F.Cu at (295.8, 56.2)
- added REF**: Pad-1U, locallib:Pad-1U, F.Cu at (295.8, 52.4)
- added REF**: Pad-1U, locallib:Pad-1U, F.Cu at (280.5, 56.7)
- added REF**: Pad-1U, locallib:Pad-1U, F.Cu at (288.1, 59.1)
- added REF**: Pad-1U, locallib:Pad-1U, F.Cu at (295.8, 60.0)
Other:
- board size 278.1 x 93.3 mm -> 341 x 93.3 mm
- board text added: "Mechanical Keyboards Ergodox"
- board text added: "Mechanical Keyboards Let's Split"
